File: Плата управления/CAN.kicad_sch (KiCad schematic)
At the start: 16 parts

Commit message: VER2.0
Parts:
- removed C18 (x3): 56p, Capacitor_SMD:C_0603_1608Metric_Pad1.08x0.95mm_HandSolder, symbol Device:C_Small
- removed C18 (x2): 1u, Capacitor_SMD:C_0603_1608Metric_Pad1.08x0.95mm_HandSolder, symbol Device:C_Small
- removed D10: SIT65HVD232DR, Package_SO:SOIC-8_3.9x4.9mm_P1.27mm, symbol CAN_My:SIT65HVD232DR
- removed D12: PESD2CAN, Package_TO_SOT_SMD:SOT-23, symbol Power_Protection:NUP2105L
- removed R30: 120, Resistor_SMD:R_0603_1608Metric_Pad0.98x0.95mm_HandSolder, symbol Device:R_Small
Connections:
- no-connect marks 4 -> 2
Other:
- note removed: "CAN 2"

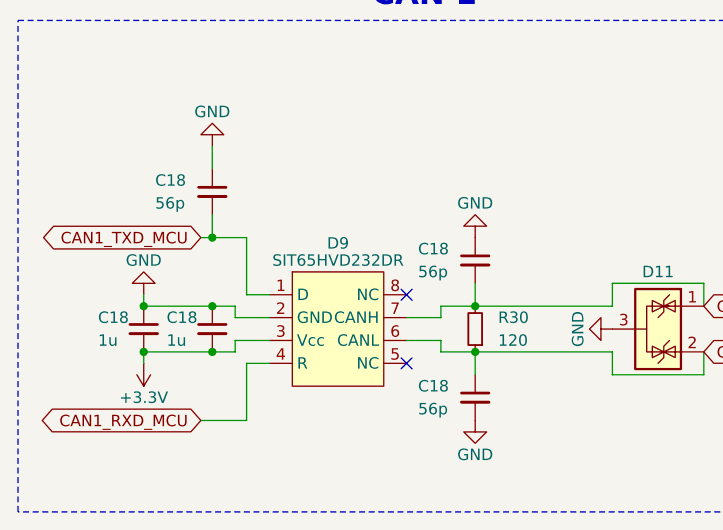
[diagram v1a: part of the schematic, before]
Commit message: Добавил NTC обработку
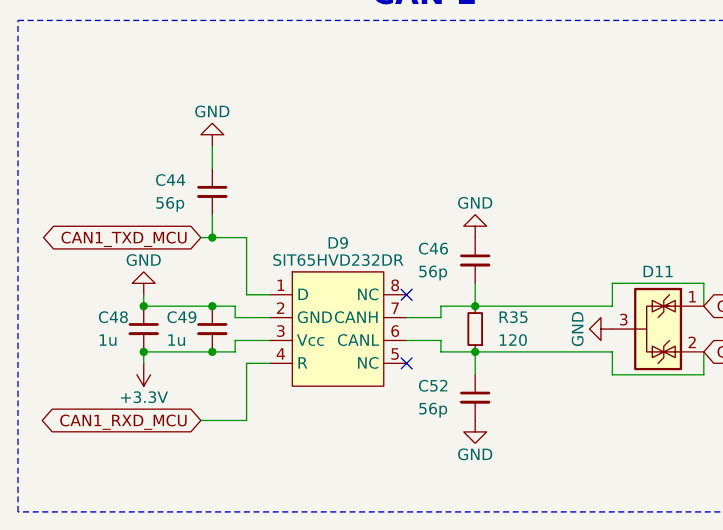
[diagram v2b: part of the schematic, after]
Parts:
- renumbered C18 to C44, C18 to C46, C18 to C48, C18 to C49, C18 to C52, R30 to R35

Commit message: Изменения: добавил папку с отчетностью
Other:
- moved on the sheet: C44, C46, C48, C49, C52, D11, D9, R35
